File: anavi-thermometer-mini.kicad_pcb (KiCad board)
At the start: 2 copper layers, 33 x 43.4 mm, 12 parts, among them SW1 SW_DIP_x01, U1 MOUDLE-SEEEDUINO-XIAO-ESP32C6, U2 DS18B20

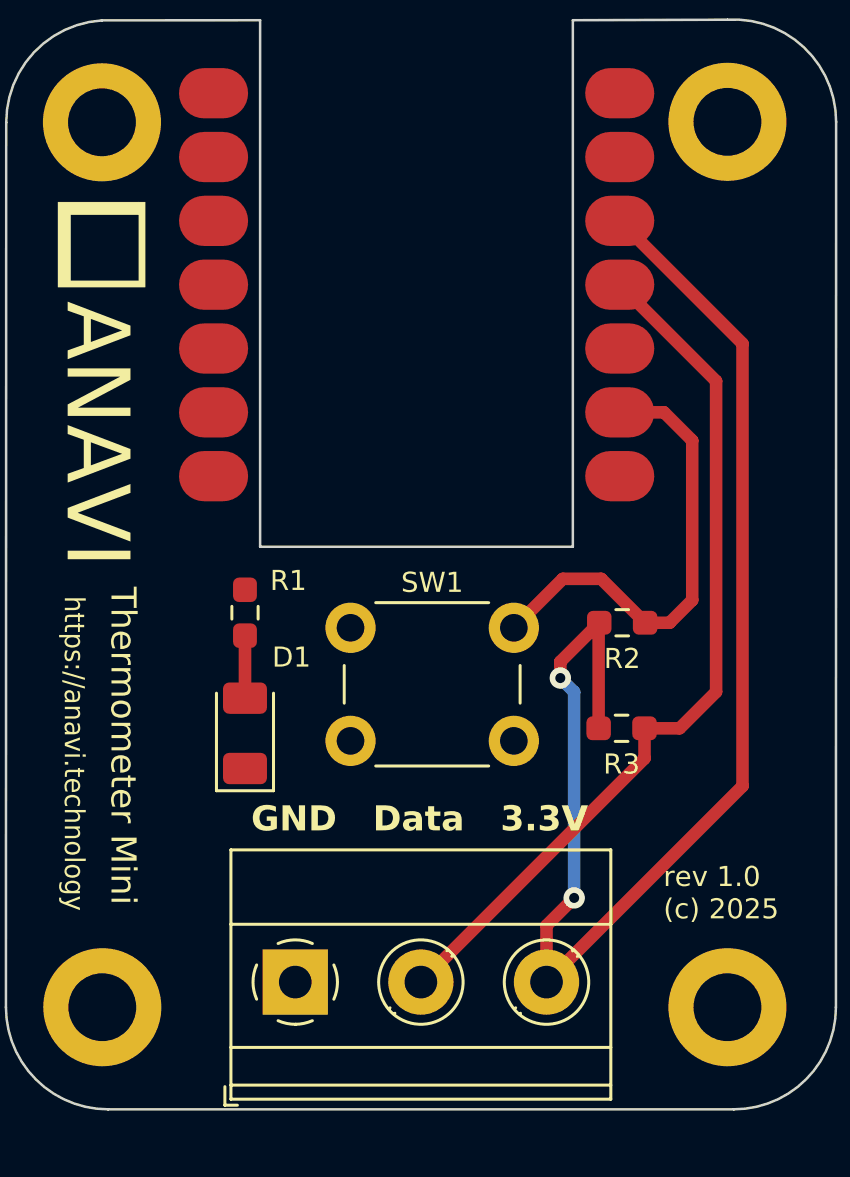
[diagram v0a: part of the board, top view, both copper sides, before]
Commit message: anavi-thermometer-mini.kicad_pcb: PCB routing
Adjust PCB routing.

Signed-off-by: Leon Anavi <leon@anavi.org>
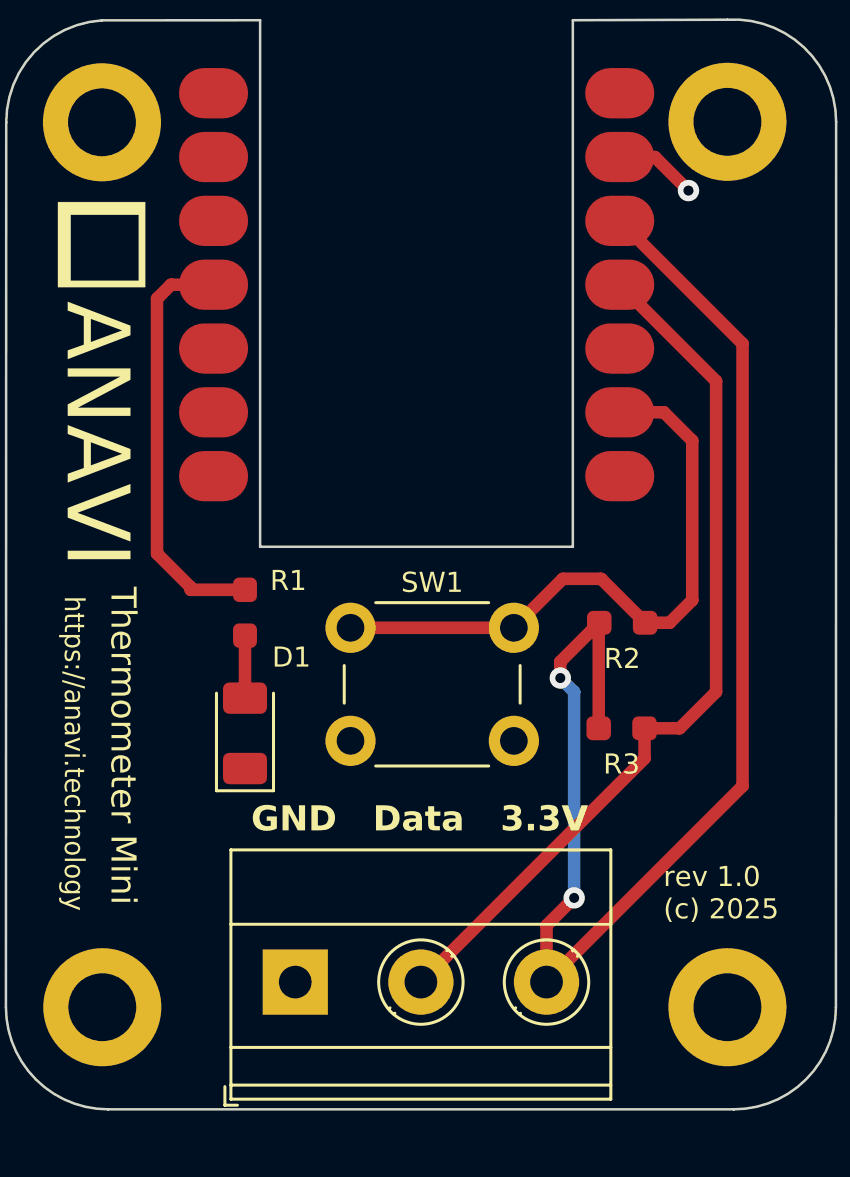
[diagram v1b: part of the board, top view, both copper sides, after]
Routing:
- net Net-(U1-PA11_A3_D3): track 0.00 -> 16.8 mm
- net Net-(U1-PA7_A8_D8_SCK): track 18.7 -> 25.2 mm
- net GND: track 0.00 -> 3.29 mm, vias 0 -> 1
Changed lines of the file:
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@@
 		(tags "resistor handsolder")
 		(property "Reference" "R2"
-			(at 0 -1.43 360)
+			(at 0 -1.43 0)
 			(layer "F.SilkS")
 			(effects
@@
 		)
 		(property "Value" "2K"
-			(at 0 1.43 360)
+			(at 0 1.43 0)
 			(layer "F.Fab")
 			(effects
@@
 		)
 		(property "Footprint" "Resistor_SMD:R_0603_1608Metric_Pad0.98x0.95mm_HandSolder"
-			(at 0 0 360)
+			(at 0 0 0)
 			(layer "F.Fab")
 			(hide yes)
@@
 		)
 		(property "Datasheet" ""
-			(at 0 0 360)
+			(at 0 0 0)
 			(layer "F.Fab")
 			(hide yes)
@@
 		)
 		(property "Description" ""
-			(at 0 0 360)
+			(at 0 0 0)
 			(layer "F.Fab")
 			(hide yes)
@@
 		(attr smd)
 		(fp_line
-			(start -0.254724 0.5225)
-			(end 0.254724 0.5225)
-			(stroke
-				(width 0.12)
-				(type solid)
-			)
-			(layer "F.SilkS")
-		)
-		(fp_line
-			(start -0.254724 -0.5225)
-			(end 0.254724 -0.5225)
-			(stroke
-				(width 0.12)
-				(type solid)
-			)
-			(layer "F.SilkS")
-		)
-		(fp_line
 			(start 1.65 0.73)
 			(end -1.65 0.73)
@@
 		)
 		(fp_text user "${REFERENCE}"
-			(at 0 0 360)
+			(at 0 0 0)
 			(layer "F.Fab")
 			(effects
@@
 		(attr smd)
 		(fp_line
-			(start -0.254724 0.5225)
-			(end 0.254724 0.5225)
-			(stroke
-				(width 0.12)
-				(type solid)
-			)
-			(layer "F.SilkS")
-		)
-		(fp_line
-			(start -0.254724 -0.5225)
-			(end 0.254724 -0.5225)
-			(stroke
-				(width 0.12)
-				(type solid)
-			)
-			(layer "F.SilkS")
-		)
-		(fp_line
 			(start -1.65 0.73)
 			(end -1.65 -0.73)
@@
 			(layer "F.SilkS")
 		)
-		(fp_arc
-			(start -1.535427 0.683042)
-			(mid -1.680501 -0.000524)
-			(end -1.535 -0.684)
-			(stroke
-				(width 0.12)
-				(type solid)
-			)
-			(layer "F.SilkS")
-		)
-		(fp_arc
-			(start -0.683042 -1.535427)
-			(mid 0.000524 -1.680501)
-			(end 0.684 -1.535)
-			(stroke
-				(width 0.12)
-				(type solid)
-			)
-			(layer "F.SilkS")
-		)
-		(fp_arc
-			(start 0.028805 1.680253)
-			(mid -0.335551 1.646659)
-			(end -0.684 1.535)
-			(stroke
-				(width 0.12)
-				(type solid)
-			)
-			(layer "F.SilkS")
-		)
-		(fp_arc
-			(start 0.683318 1.534756)
-			(mid 0.349292 1.643288)
-			(end 0 1.68)
-			(stroke
-				(width 0.12)
-				(type solid)
-			)
-			(layer "F.SilkS")
-		)
-		(fp_arc
-			(start 1.535427 -0.683042)
-			(mid 1.680501 0.000524)
-			(end 1.535 0.684)
-			(stroke
-				(width 0.12)
-				(type solid)
-			)
-			(layer "F.SilkS")
-		)
 		(fp_circle
 			(center 5 0)
@@
 		(tags "resistor handsolder")
 		(property "Reference" "R3"
-			(at 0 -1.43 360)
+			(at 0 -1.43 0)
 			(layer "F.SilkS")
 			(effects
@@
 		)
 		(property "Value" "4,7K"
-			(at 0 1.43 360)
+			(at 0 1.43 0)
 			(layer "F.Fab")
 			(effects
@@
 		)
 		(property "Footprint" "Resistor_SMD:R_0603_1608Metric_Pad0.98x0.95mm_HandSolder"
-			(at 0 0 360)
+			(at 0 0 0)
 			(layer "F.Fab")
 			(hide yes)
@@
 		)
 		(property "Datasheet" ""
-			(at 0 0 360)
+			(at 0 0 0)
 			(layer "F.Fab")
 			(hide yes)
@@
 		)
 		(property "Description" ""
-			(at 0 0 360)
+			(at 0 0 0)
 			(layer "F.Fab")
 			(hide yes)
@@
 		(attr smd)
 		(fp_line
-			(start -0.254724 0.5225)
-			(end 0.254724 0.5225)
-			(stroke
-				(width 0.12)
-				(type solid)
-			)
-			(layer "F.SilkS")
-		)
-		(fp_line
-			(start -0.254724 -0.5225)
-			(end 0.254724 -0.5225)
-			(stroke
-				(width 0.12)
-				(type solid)
-			)
-			(layer "F.SilkS")
-		)
-		(fp_line
 			(start 1.65 0.73)
 			(end -1.65 0.73)
@@
 		)
 		(fp_text user "${REFERENCE}"
-			(at 0 0 360)
+			(at 0 0 0)
 			(layer "F.Fab")
 			(effects
@@
 	)
 	(segment
+		(start 157.314 38.46525)
+		(end 158.71525 38.46525)
+		(width 0.5)
+		(layer "F.Cu")
+		(net 1)
+	)
+	(segment
+		(start 158.71525 38.46525)
+		(end 160.05 39.8)
+		(width 0.5)
+		(layer "F.Cu")
+		(net 1)
+	)
+	(via
+		(at 160.05 39.8)
+		(size 0.85)
+		(drill 0.4)
+		(layers "F.Cu" "B.Cu")
+		(net 1)
+	)
+	(segment
 		(start 142.4 57.5125)
 		(end 142.4 60)
@@
 	)
 	(segment
+		(start 140.2375 55.5875)
+		(end 138.9 54.25)
+		(width 0.5)
+		(layer "F.Cu")
+		(net 3)
+	)
+	(segment
+		(start 139.45475 43.54525)
+		(end 138.9 44.1)
+		(width 0.5)
+		(layer "F.Cu")
+		(net 3)
+	)
+	(segment
+		(start 141.149 43.54525)
+		(end 139.45475 43.54525)
+		(width 0.5)
+		(layer "F.Cu")
+		(net 3)
+	)
+	(segment
+		(start 140.2375 55.6875)
+		(end 142.4 55.6875)
+		(width 0.5)
+		(layer "F.Cu")
+		(net 3)
+	)
+	(segment
+		(start 140.2375 55.6875)
+		(end 140.2375 55.5875)
+		(width 0.5)
+		(layer "F.Cu")
+		(net 3)
+	)
+	(segment
+		(start 138.9 44.1)
+		(end 138.9 54.25)
+		(width 0.5)
+		(layer "F.Cu")
+		(net 3)
+	)
+	(segment
 		(start 156.475 61.2)
 		(end 156.475 57.025)
@@
 		(width 0.5)
 		(layer "F.Cu")
+		(net 5)
+	)
+	(segment
+		(start 153.1 57.2)
+		(end 146.6 57.2)
+		(width 0.5)
+		(layer "F.Cu")

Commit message: Minor adjustments of the PCB
Signed-off-by: Leon Anavi <leon@anavi.org>
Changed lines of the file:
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@@
 		)
 	)
-	(gr_text "GND   Data   3.3V"
-		(at 149.35 64.8 0)
+	(gr_text "GND  Data   3.3V"
+		(at 149.375 64.85 0)
 		(layer "F.SilkS")
 		(effects
